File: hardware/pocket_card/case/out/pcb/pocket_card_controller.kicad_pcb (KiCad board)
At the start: 2 copper layers, 75 x 37 mm, 21 parts, among them U1 SOIC-28W_7.5x17.9mm_P1.27mm

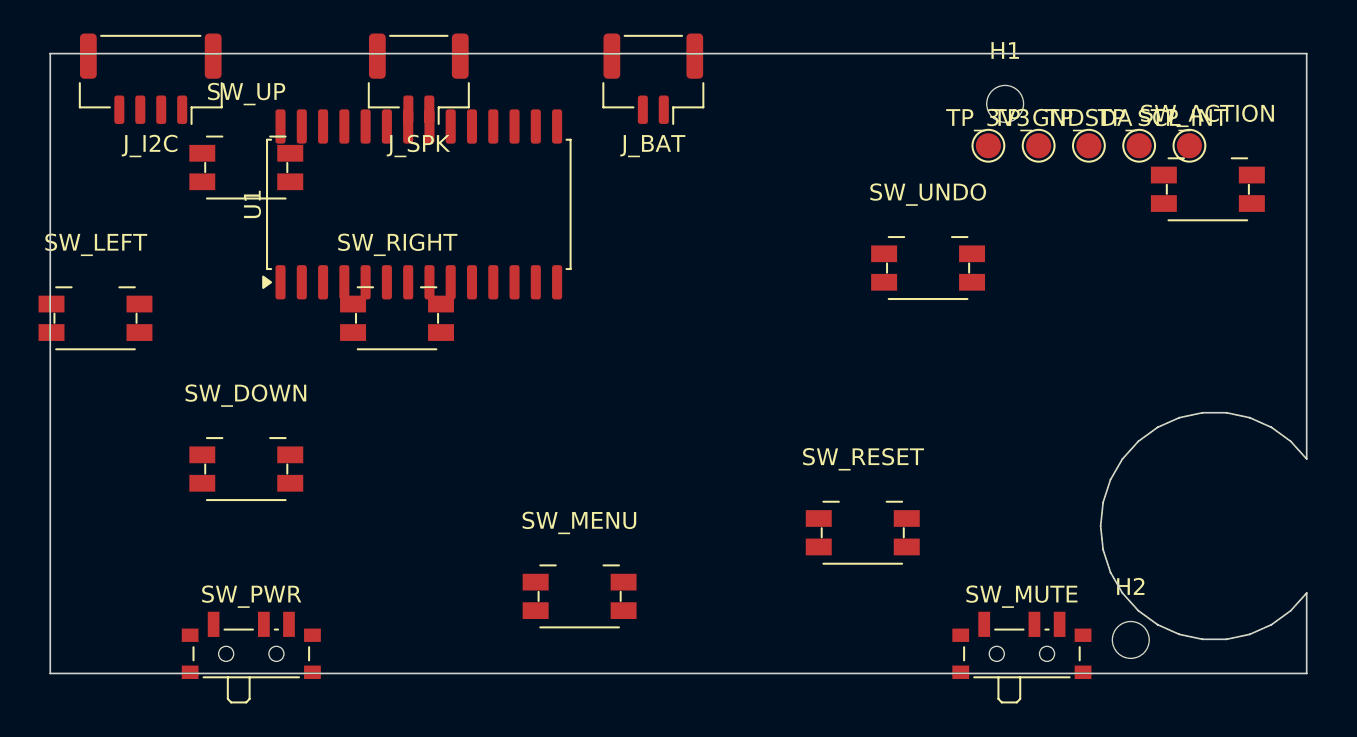
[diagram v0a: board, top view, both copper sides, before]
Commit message: Correct the controller PCB connector complement and mounting
The connectors were wrong. The board needs:
  J_I2C      4P  3V3/GND/SCL/SDA, to the module's I2C socket
  J_EXP      4P  IO2 as the expander interrupt, to the expansion socket
  J_BAT_IN   2P  from the cell
  J_BAT_OUT  2P  to the module's BAT socket

Two battery connectors, not one: the power switch sits IN the cell lead,
so the board has to break that circuit rather than tap it.

The speaker does not pass through this board at all. Mute is a logic
signal to the module's amp-enable pin, not a break in the speaker wires,
so the driver wires straight to the module.

Mounting holes move to (65,56) and (80,72). Both are on the right
because the cell fence reaches x=60.8 and a screw cannot land where the
cell is behind the board. The left edge needs a retaining lip on the
front shell instead -- not yet modelled.

Co-Authored-By: Claude Opus 5 <noreply@anthropic.com>
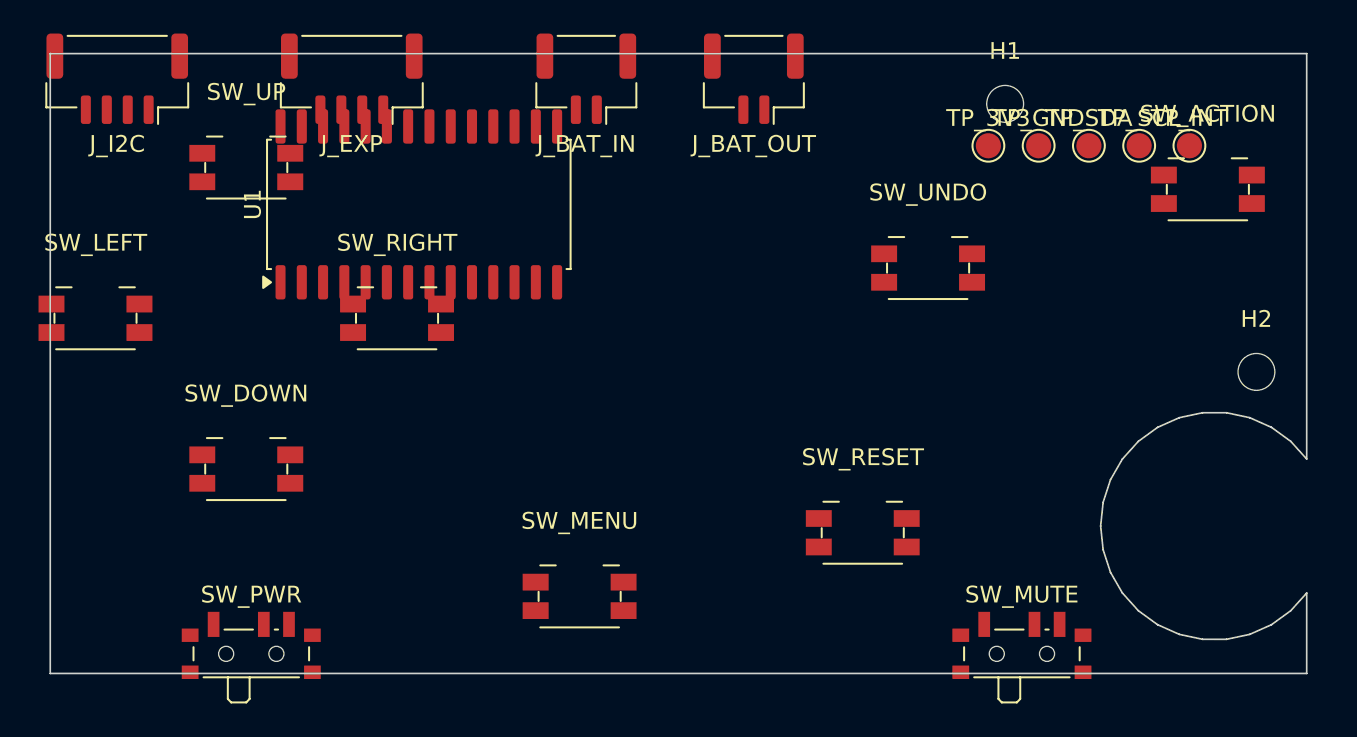
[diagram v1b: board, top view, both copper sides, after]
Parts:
- removed J_BAT, J_SPK: JST_GH_SM02B-GHS-TB_1x02-1MP_P1.25mm_Horizontal, JST_GH_SM02B-GHS-TB_1x02-1MP_P1.25mm_Horizontal
- added J_BAT_IN: JST_GH_SM02B-GHS-TB_1x02-1MP_P1.25mm_Horizontal, JST_GH_SM02B-GHS-TB_1x02-1MP_P1.25mm_Horizontal, F.Cu at (40.0, 54.5)
- added J_BAT_OUT: JST_GH_SM02B-GHS-TB_1x02-1MP_P1.25mm_Horizontal, JST_GH_SM02B-GHS-TB_1x02-1MP_P1.25mm_Horizontal, F.Cu at (50.0, 54.5)
- added J_EXP: JST_GH_SM04B-GHS-TB_1x04-1MP_P1.25mm_Horizontal, JST_GH_SM04B-GHS-TB_1x04-1MP_P1.25mm_Horizontal, F.Cu at (26.0, 54.5)
- moved H2 17.7 mm to (80.0, 72.0)
- moved J_I2C 2.00 mm to (12.0, 54.5)

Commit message: Move U1 clear of the button collars; record routing as unsolved
U1 sat at (30,62) rotated 90, where the SOIC-28 package overlapped the
'up' and 'right' direction collars in plan. Components sit at z 3.75-5.5
and the collars end at 3.5, so that is a real collision, not just a
drawing overlap. Moved to (45,72) unrotated, which is clear of all
seven collar footprints.

pcb_route.py assigns nets, chooses the expander GPIO allocation by
geometry and pours ground -- but its routing FAILS DRC: 83 violations
and 26 unconnected, including nets shorted by ground vias dropped on
pad centres and back-layer traces crossing undetected. Committed as a
record of the approach, not as working output. The board file itself is
regenerated as clean placement so nothing broken ships.

Next: pcbnew exposes ExportSpecctraDSN and ImportSpecctraSES, and Java
is present, so the standard freerouting workflow is available and is
the right tool. Hand-rolling a router was not.

Co-Authored-By: Claude Opus 5 <noreply@anthropic.com>
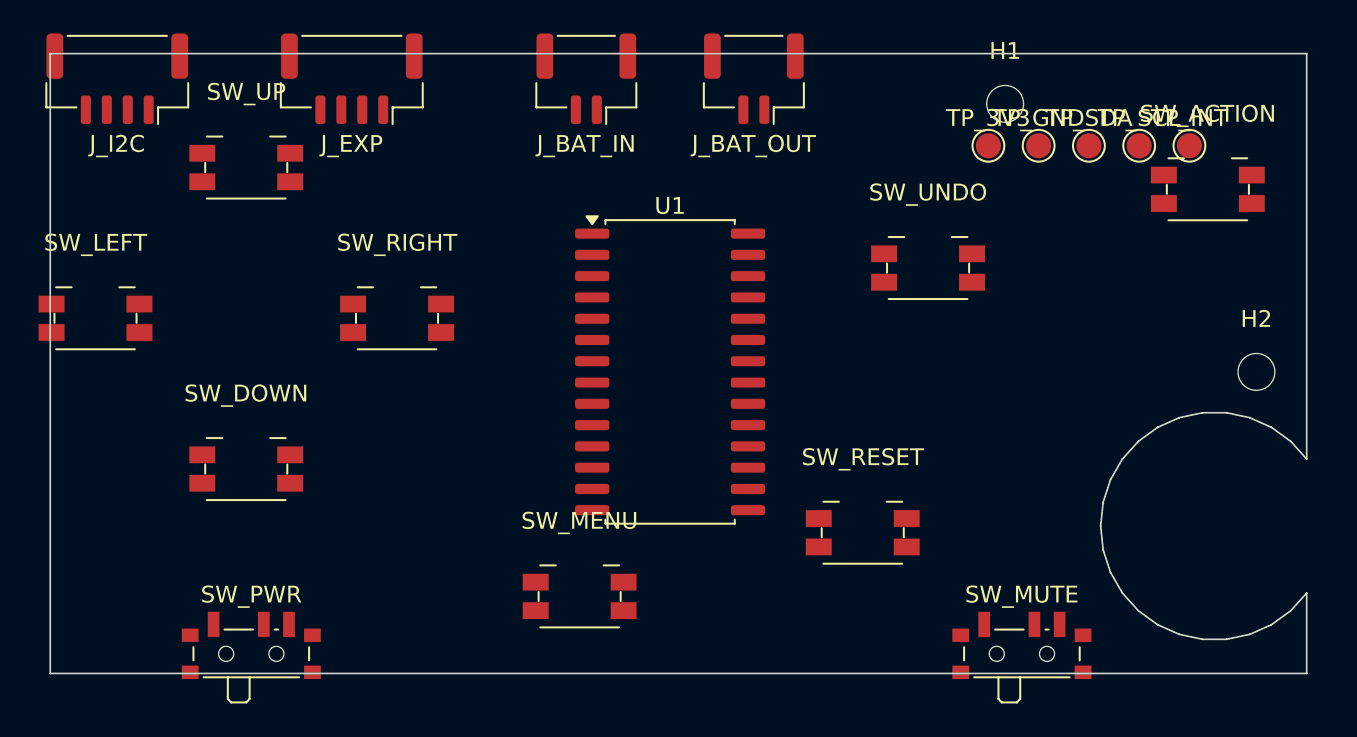
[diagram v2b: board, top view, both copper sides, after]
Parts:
- moved U1 18.0 mm to (45.0, 72.0), turned to 0 degrees

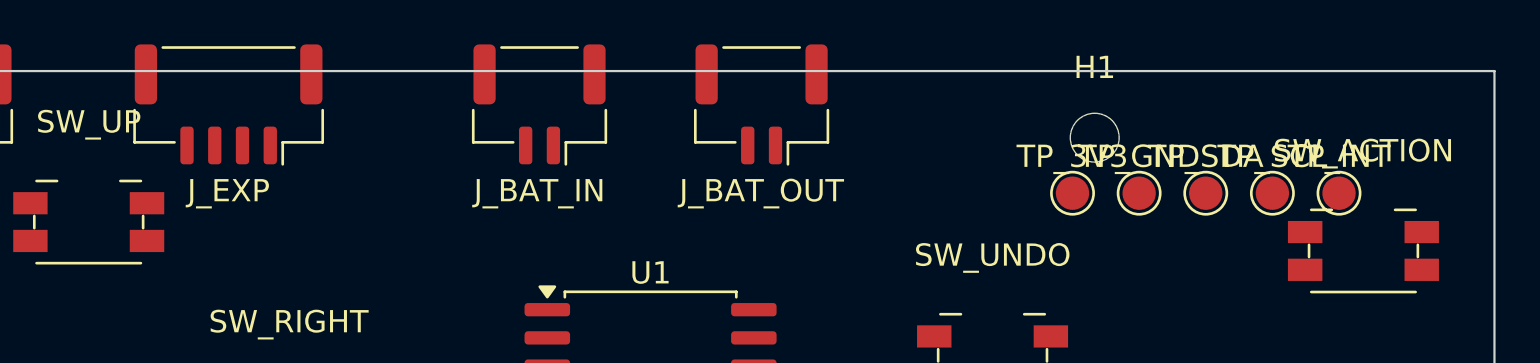
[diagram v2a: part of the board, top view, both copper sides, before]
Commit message: Route the controller PCB with freerouting instead of by hand
Hand-rolled routing produced 83 DRC violations including shorted nets
and crossing tracks. Freerouting via Specctra DSN/SES produced zero of
either. That approach is settled; the remaining work is inputs.

Three of my own errors fixed along the way:

  - The ground pour was B.Cu only, which cannot reach front-side SMD
    pads, leaving every switch common floating. 38 of the reported
    unconnected items were GND. Now poured on both layers.
  - The test-point row collided with SW_ACTION and mounting hole H1.
    Deleted rather than moved: J_I2C already exposes 3V3, GND, SCL and
    SDA on 1.25 mm pads and J_EXP exposes the interrupt, so it bought
    nothing.
  - No design rules were set. A board from CreateEmptyBoard carries
    defaults too coarse for this fanout, and freerouting honours what
    the DSN declares -- with them it left 24 nets unrouted. Now 0.2 mm
    track, 0.15 mm clearance, 0.6/0.3 via.

Also passes -mt 1, since freerouting's own log warns its multi-threaded
optimiser is broken and generates clearance violations.

Still not orderable: DRC must come back clean first.

Co-Authored-By: Claude Opus 5 <noreply@anthropic.com>
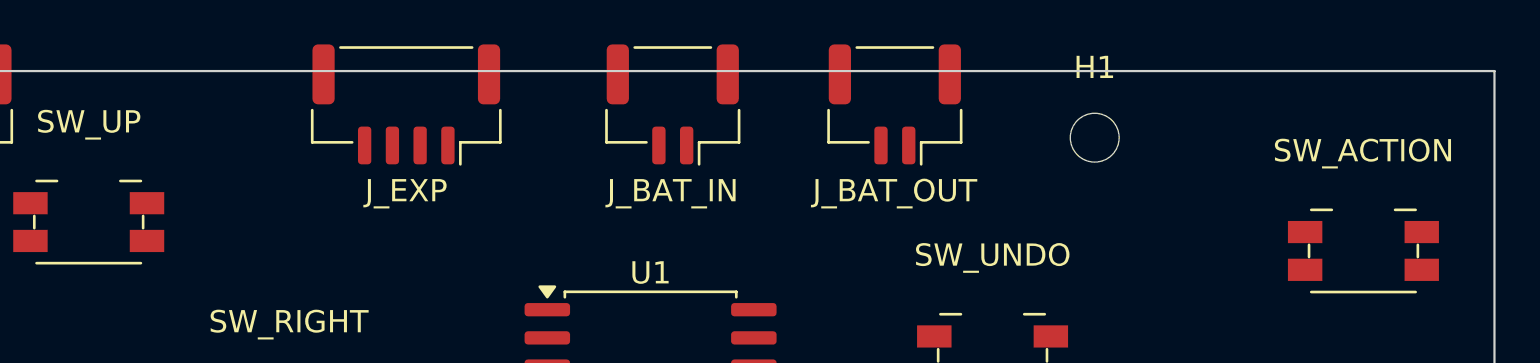
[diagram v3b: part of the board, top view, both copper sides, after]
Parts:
- removed TP_3V3, TP_GND, TP_INT, TP_SCL, TP_SDA: TestPoint_Pad_D1.5mm, TestPoint_Pad_D1.5mm
- moved J_EXP 8.00 mm to (34.0, 54.5)
- moved J_BAT_IN 6.00 mm to (46.0, 54.5)
- moved J_BAT_OUT 6.00 mm to (56.0, 54.5)
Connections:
- J_BAT_IN pad 1: (no net) -> BAT_P
- J_BAT_IN pad 2: (no net) -> GND
- J_BAT_OUT pad 1: (no net) -> BAT_SW
- J_BAT_OUT pad 2: (no net) -> GND
- J_EXP pad 1: (no net) -> INT
- J_I2C pad 1: (no net) -> +3V3
- J_I2C pad 2: (no net) -> GND
- J_I2C pad 3: (no net) -> SCL
- J_I2C pad 4: (no net) -> SDA
- SW_ACTION pad 1: (no net) -> GND
- SW_ACTION pad 2: (no net) -> GND
- SW_DOWN pad 1: (no net) -> GND
- SW_DOWN pad 2: (no net) -> GND
- SW_LEFT pad 1: (no net) -> GND
- SW_LEFT pad 2: (no net) -> GND
- SW_MENU pad 1: (no net) -> GND
- SW_MENU pad 2: (no net) -> GND
- SW_MUTE pad : (no net) -> GND
- SW_MUTE pad 1: (no net) -> GND
- SW_MUTE pad 2: (no net) -> GND
- SW_MUTE pad 3: (no net) -> GND
- SW_PWR pad 1: (no net) -> BAT_SW
- SW_PWR pad 2: (no net) -> BAT_P
- SW_RESET pad 1: (no net) -> GND
- SW_RESET pad 2: (no net) -> GND
- SW_RIGHT pad 1: (no net) -> GND
- SW_RIGHT pad 2: (no net) -> GND
- SW_UNDO pad 1: (no net) -> GND
- SW_UNDO pad 2: (no net) -> GND
- SW_UP pad 1: (no net) -> GND
- SW_UP pad 2: (no net) -> GND
- U1 pad 1: (no net) -> SIG_UP
- U1 pad 10: (no net) -> GND
- U1 pad 12: (no net) -> SCL
- U1 pad 13: (no net) -> SDA
- U1 pad 15: (no net) -> GND
- U1 pad 16: (no net) -> GND
- U1 pad 17: (no net) -> GND
- U1 pad 18: (no net) -> +3V3
- U1 pad 20: (no net) -> INT
- U1 pad 21: (no net) -> SIG_DOWN
- U1 pad 22: (no net) -> SIG_RESET
- U1 pad 23: (no net) -> SIG_MENU
- U1 pad 24: (no net) -> SIG_LEFT
- U1 pad 25: (no net) -> SIG_RIGHT
- U1 pad 26: (no net) -> SIG_UNDO
- U1 pad 27: (no net) -> SIG_MUTE
- U1 pad 28: (no net) -> SIG_ACTION
- U1 pad 9: (no net) -> +3V3

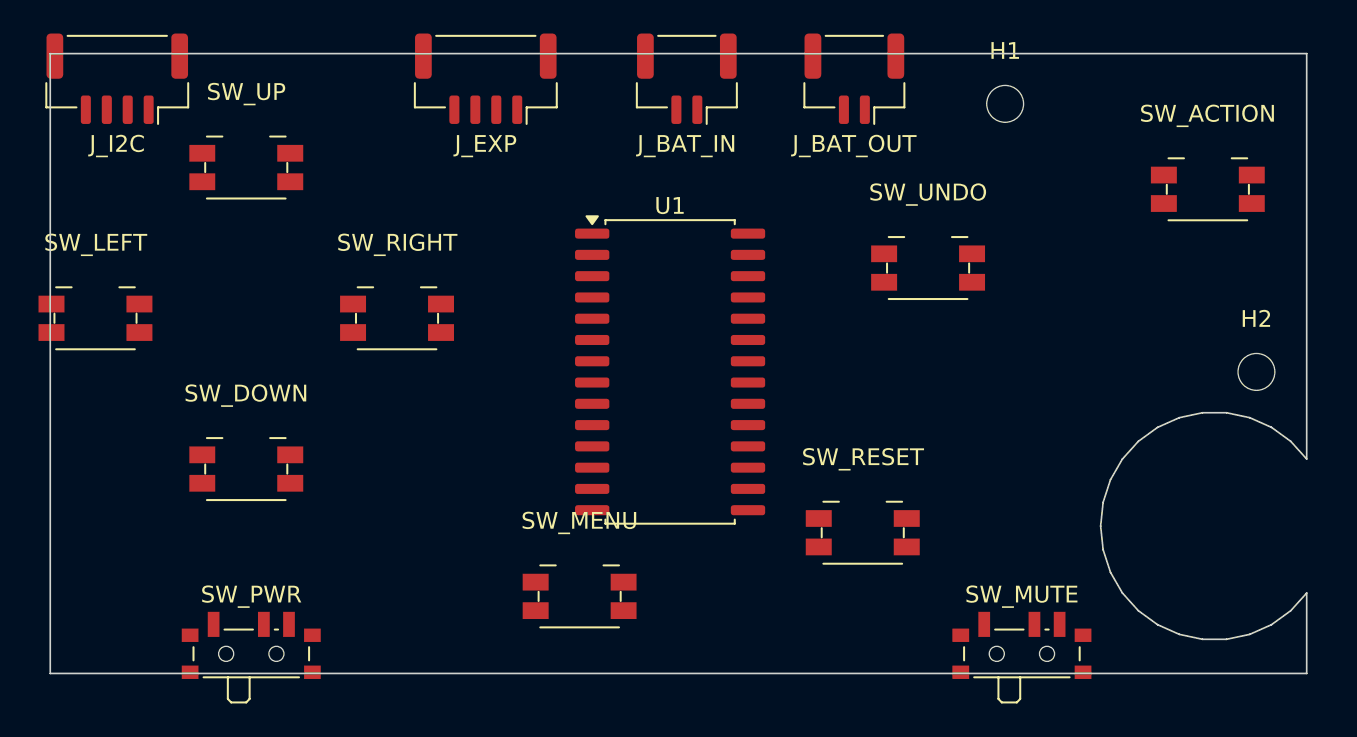
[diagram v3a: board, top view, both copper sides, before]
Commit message: Autorouting pipeline runs end to end; ground remains unsolved
The pipeline now completes: nets assigned, DSN exported, freerouting
invoked, SES imported, board saved. 50 tracks, 4 vias, 17 nets.

Signals route. Ground does not. Every GND connection is left for
freerouting to wire point-to-point -- roughly 25 of them on two layers
-- and it gives up, which is what the ~40 unrouted nets are. A copper
pour would make this trivial and is the normal answer.

The pour is blocked: board.Save() segfaults whenever a zone is present.
Reproducible, no traceback, and uncatchable because a segfault takes the
interpreter with it. Setting the zone defaults that a bare pcbnew.ZONE()
lacks (min thickness, priority, and a non-zero hatch pitch via
SetBorderDisplayStyle) makes a minimal standalone script save correctly,
but not this one. I did not isolate the difference.

Fixed along the way and worth keeping:
  - wx.App() must exist before ZONE_FILLER or pcbnew segfaults
  - switch pads must be netted by pad NAME; this footprint has two pads
    called 1 and two called 2, so indexing shorted signal to ground
    through the switch itself

The board is NOT orderable. Placement and netlist are correct; routing
is incomplete.

Co-Authored-By: Claude Opus 5 <noreply@anthropic.com>
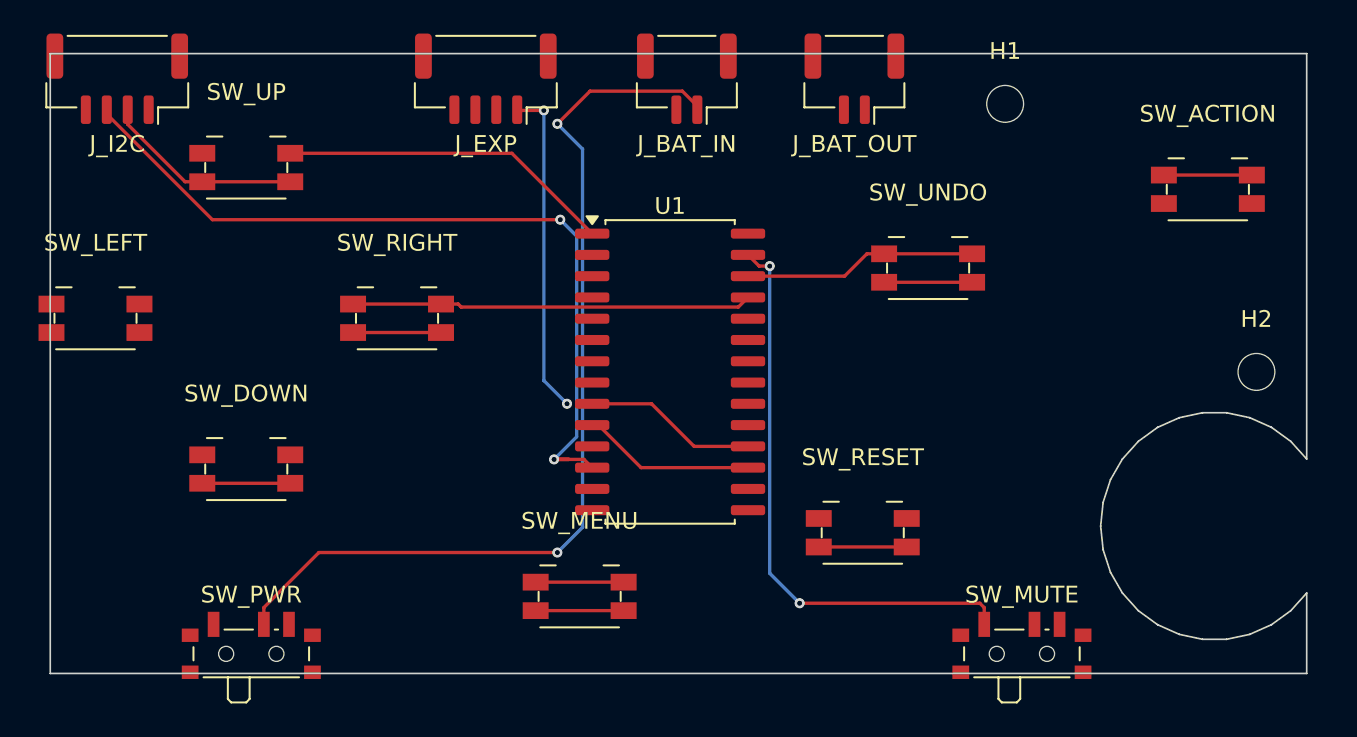
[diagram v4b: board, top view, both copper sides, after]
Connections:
- SW_ACTION pad 1: GND -> SIG_ACTION
- SW_DOWN pad 1: GND -> SIG_DOWN
- SW_LEFT pad 1: GND -> SIG_LEFT
- SW_MENU pad 1: GND -> SIG_MENU
- SW_MUTE pad 1: GND -> SIG_MUTE
- SW_RESET pad 1: GND -> SIG_RESET
- SW_RIGHT pad 1: GND -> SIG_RIGHT
- SW_UNDO pad 1: GND -> SIG_UNDO
- SW_UP pad 1: GND -> SIG_UP
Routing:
- net BAT_P: track 0.00 -> 56.5 mm, vias 0 -> 2
- net SCL: track 0.00 -> 51.2 mm, vias 0 -> 2
- net GND: track 0.00 -> 48.6 mm
- net SIG_MUTE: track 0.00 -> 34.6 mm, vias 0 -> 2
- net SIG_RIGHT: track 0.00 -> 23.9 mm
- net SIG_UP: track 0.00 -> 20.0 mm
- net INT: track 0.00 -> 19.7 mm, vias 0 -> 2
- net SIG_UNDO: track 0.00 -> 13.9 mm
- net +3V3: track 0.00 -> 10.4 mm
- net SIG_MENU: track 0.00 -> 5.25 mm
- net SIG_ACTION: track 0.00 -> 5.25 mm
